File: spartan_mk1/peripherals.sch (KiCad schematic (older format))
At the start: 10 parts

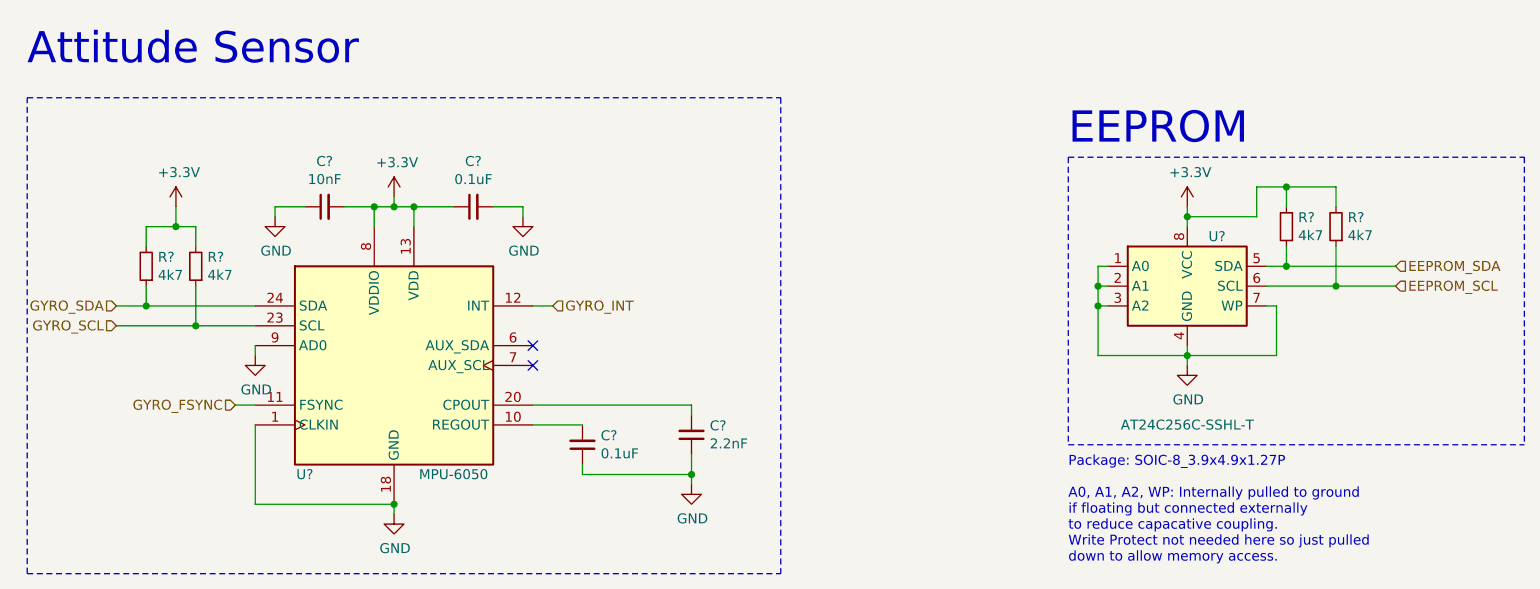
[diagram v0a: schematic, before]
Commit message: Complete schematic with DRC done
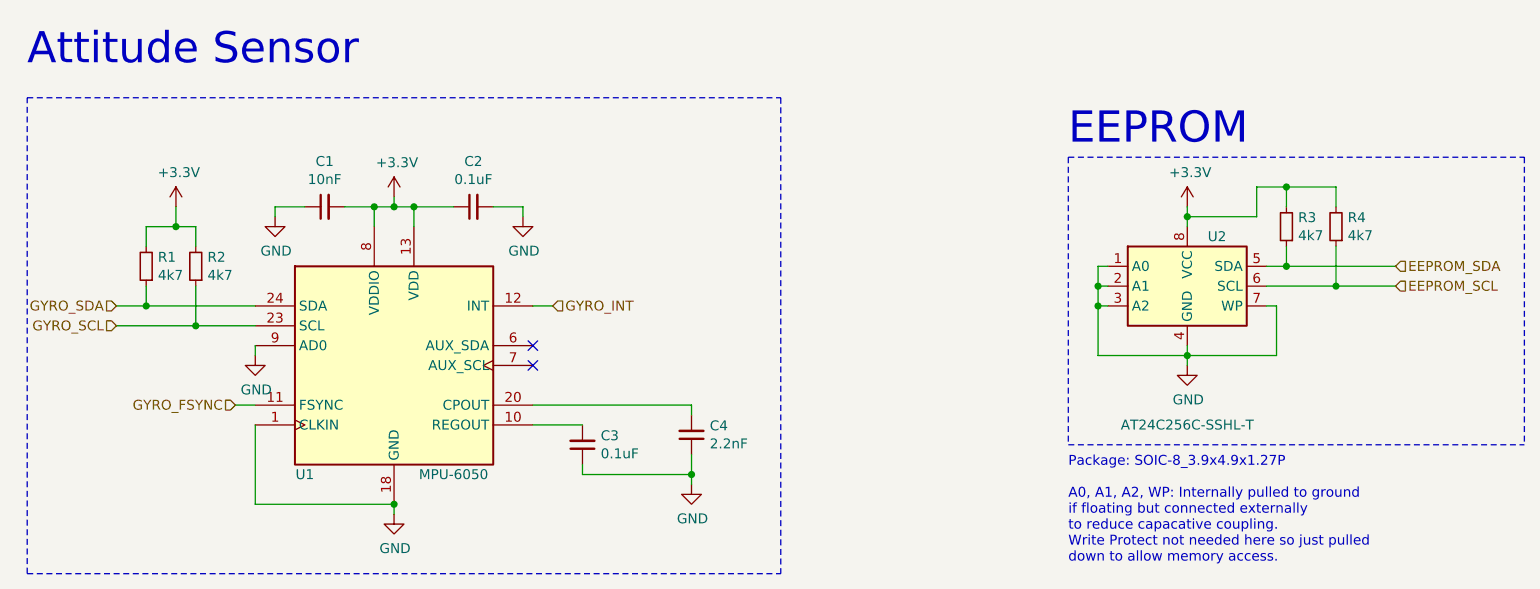
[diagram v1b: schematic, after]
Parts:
- gave numbers to parts that had none: 10
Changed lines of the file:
@@
 	4250 3550 4150 3550
 $Comp
-L Device:C_Small C?
+L Device:C_Small C3
 U 1 1 5F7B41B1
 P 4400 4250
-F 0 "C?" H 4308 4204 50  0000 R CNN
+F 0 "C3" H 4308 4204 50  0000 R CNN
 F 1 "0.1uF" H 4308 4295 50  0000 R CNN
 F 2 "" H 4400 4250 50  0001 C CNN
@@
 $EndComp
 $Comp
-L Device:C_Small C?
+L Device:C_Small C4
 U 1 1 5F7B5CAE
 P 4950 4200
-F 0 "C?" H 4858 4154 50  0000 R CNN
+F 0 "C4" H 4858 4154 50  0000 R CNN
 F 1 "2.2nF" H 4858 4245 50  0000 R CNN
 F 2 "" H 4950 4200 50  0001 C CNN
@@
 	4400 4150 4150 4150
 $Comp
-L Device:C_Small C?
+L Device:C_Small C2
 U 1 1 5F7B64CF
 P 3850 3050
-F 0 "C?" V 4079 3050 50  0000 C CNN
+F 0 "C2" V 4079 3050 50  0000 C CNN
 F 1 "0.1uF" V 3988 3050 50  0000 C CNN
 F 2 "" H 3850 3050 50  0001 C CNN
@@
 $EndComp
 $Comp
-L Device:C_Small C?
+L Device:C_Small C1
 U 1 1 5F7B8C83
 P 3100 3050
-F 0 "C?" V 3329 3050 50  0000 C CNN
+F 0 "C1" V 3329 3050 50  0000 C CNN
 F 1 "10nF" V 3238 3050 50  0000 C CNN
 F 2 "" H 3100 3050 50  0001 C CNN
@@
 $EndComp
 $Comp
-L power:GND #PWR?
+L power:GND #PWR06
 U 1 1 5F7B9C5E
 P 4100 3100
-F 0 "#PWR?" H 4100 2850 50  0001 C CNN
+F 0 "#PWR06" H 4100 2850 50  0001 C CNN
 F 1 "GND" H 4105 2927 50  0000 C CNN
 F 2 "" H 4100 3100 50  0001 C CNN
@@
 	4100 3050 3950 3050
 $Comp
-L power:GND #PWR?
+L power:GND #PWR07
 U 1 1 5F7BA737
 P 4950 4450
-F 0 "#PWR?" H 4950 4200 50  0001 C CNN
+F 0 "#PWR07" H 4950 4200 50  0001 C CNN
 F 1 "GND" H 4955 4277 50  0000 C CNN
 F 2 "" H 4950 4450 50  0001 C CNN
@@
 	4400 4400 4400 4350
 $Comp
-L power:+3.3V #PWR?
+L power:+3.3V #PWR04
 U 1 1 5F7BB185
 P 3450 3000
-F 0 "#PWR?" H 3450 2850 50  0001 C CNN
+F 0 "#PWR04" H 3450 2850 50  0001 C CNN
 F 1 "+3.3V" H 3465 3173 50  0000 C CNN
 F 2 "" H 3450 3000 50  0001 C CNN
@@
 	3350 3050 3200 3050
 $Comp
-L power:GND #PWR?
+L power:GND #PWR03
 U 1 1 5F7BC050
 P 2850 3100
-F 0 "#PWR?" H 2850 2850 50  0001 C CNN
+F 0 "#PWR03" H 2850 2850 50  0001 C CNN
 F 1 "GND" H 2855 2927 50  0000 C CNN
 F 2 "" H 2850 3100 50  0001 C CNN
@@
 	2650 4050 2750 4050
 $Comp
-L power:GND #PWR?
+L power:GND #PWR05
 U 1 1 5F7BD9F9
 P 3450 4600
-F 0 "#PWR?" H 3450 4350 50  0001 C CNN
+F 0 "#PWR05" H 3450 4350 50  0001 C CNN
 F 1 "GND" H 3455 4427 50  0000 C CNN
 F 2 "" H 3450 4600 50  0001 C CNN
@@
 	3450 4550 2750 4550
 $Comp
-L Sensor_Motion:MPU-6050 U?
+L Sensor_Motion:MPU-6050 U1
 U 1 1 5F78649D
 P 3450 3850
-F 0 "U?" H 3000 3300 50  0000 C CNN
+F 0 "U1" H 3000 3300 50  0000 C CNN
 F 1 "MPU-6050" H 3750 3300 50  0000 C CNN
 F 2 "Sensor_Motion:InvenSense_QFN-24_4x4mm_P0.5mm" H 3450 3050 50  0001 C CNN
@@
 $EndComp
 $Comp
-L power:GND #PWR?
+L power:GND #PWR02
 U 1 1 5F993355
 P 2750 3800
-F 0 "#PWR?" H 2750 3550 50  0001 C CNN
+F 0 "#PWR02" H 2750 3550 50  0001 C CNN
 F 1 "GND" H 2755 3627 50  0000 C CNN
 F 2 "" H 2750 3800 50  0001 C CNN
@@
 	2750 3800 2750 3750
 $Comp
-L power:+3.3V #PWR?
+L power:+3.3V #PWR01
 U 1 1 5F993AD9
 P 2350 3050
-F 0 "#PWR?" H 2350 2900 50  0001 C CNN
+F 0 "#PWR01" H 2350 2900 50  0001 C CNN
 F 1 "+3.3V" H 2365 3223 50  0000 C CNN
 F 2 "" H 2350 3050 50  0001 C CNN
@@
 $EndComp
 $Comp
-L Device:R_Small R?
+L Device:R_Small R2
 U 1 1 5F994B07
 P 2450 3350
-F 0 "R?" H 2391 3304 50  0000 R CNN
+F 0 "R2" H 2391 3304 50  0000 R CNN
 F 1 "4k7" H 2391 3395 50  0000 R CNN
 F 2 "" H 2450 3350 50  0001 C CNN
@@
 $EndComp
 $Comp
-L Device:R_Small R?
+L Device:R_Small R1
 U 1 1 5F995818
 P 2200 3350
-F 0 "R?" H 2141 3304 50  0000 R CNN
+F 0 "R1" H 2141 3304 50  0000 R CNN
 F 1 "4k7" H 2141 3395 50  0000 R CNN
 F 2 "" H 2200 3350 50  0001 C CNN
@@
 EEPROM
 $Comp
-L Memory_EEPROM:AT24CS64-SSHM U?
+L Memory_EEPROM:AT24CS64-SSHM U2
 U 1 1 5F9AB042
 P 7450 3450
-F 0 "U?" H 7600 3700 50  0000 C CNN
+F 0 "U2" H 7600 3700 50  0000 C CNN
 F 1 "AT24C256C-SSHL-T" H 7450 2750 50  0000 C CNN
 F 2 "Package_SO:SOIC-8_3.9x4.9mm_P1.27mm" H 7450 3450 50  0001 C CNN
@@
 $EndComp
 $Comp
-L power:GND #PWR?
+L power:GND #PWR09
 U 1 1 5F9AC2AC
 P 7450 3850
-F 0 "#PWR?" H 7450 3600 50  0001 C CNN
+F 0 "#PWR09" H 7450 3600 50  0001 C CNN
 F 1 "GND" H 7455 3677 50  0000 C CNN
 F 2 "" H 7450 3850 50  0001 C CNN
@@
 Package: SOIC-8_3.9x4.9x1.27P\n\nA0, A1, A2, WP: Internally pulled to ground \nif floating but connected externally \nto reduce capacative coupling. \nWrite Protect not needed here so just pulled \ndown to allow memory access.\n
 $Comp
-L power:+3.3V #PWR?
+L power:+3.3V #PWR08
 U 1 1 5F9B2229
 P 7450 3050
-F 0 "#PWR?" H 7450 2900 50  0001 C CNN
+F 0 "#PWR08" H 7450 2900 50  0001 C CNN
 F 1 "+3.3V" H 7465 3223 50  0000 C CNN
 F 2 "" H 7450 3050 50  0001 C CNN
@@
 EEPROM_SCL
 $Comp
-L Device:R_Small R?
+L Device:R_Small R4
 U 1 1 5F9C0959
 P 8200 3150
-F 0 "R?" H 8141 3104 50  0000 R CNN
+F 0 "R4" H 8141 3104 50  0000 R CNN
 F 1 "4k7" H 8141 3195 50  0000 R CNN
 F 2 "" H 8200 3150 50  0001 C CNN
@@
 $EndComp
 $Comp
-L Device:R_Small R?
+L Device:R_Small R3
 U 1 1 5F9C095F
 P 7950 3150
-F 0 "R?" H 7891 3104 50  0000 R CNN
+F 0 "R3" H 7891 3104 50  0000 R CNN
 F 1 "4k7" H 7891 3195 50  0000 R CNN
 F 2 "" H 7950 3150 50  0001 C CNN

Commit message: Footprints added started PCB placement
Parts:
- C1, C2, C3, C4: footprint (none) -> Capacitor_SMD:C_0402_1005Metric
- R1, R2, R3, R4: footprint (none) -> Resistor_SMD:R_0402_1005Metric
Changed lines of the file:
@@
 F 0 "C3" H 4308 4204 50  0000 R CNN
 F 1 "0.1uF" H 4308 4295 50  0000 R CNN
-F 2 "" H 4400 4250 50  0001 C CNN
+F 2 "Capacitor_SMD:C_0402_1005Metric" H 4400 4250 50  0001 C CNN
 F 3 "~" H 4400 4250 50  0001 C CNN
 	1    4400 4250
@@
 F 0 "C4" H 4858 4154 50  0000 R CNN
 F 1 "2.2nF" H 4858 4245 50  0000 R CNN
-F 2 "" H 4950 4200 50  0001 C CNN
+F 2 "Capacitor_SMD:C_0402_1005Metric" H 4950 4200 50  0001 C CNN
 F 3 "~" H 4950 4200 50  0001 C CNN
 	1    4950 4200
@@
 F 0 "C2" V 4079 3050 50  0000 C CNN
 F 1 "0.1uF" V 3988 3050 50  0000 C CNN
-F 2 "" H 3850 3050 50  0001 C CNN
+F 2 "Capacitor_SMD:C_0402_1005Metric" H 3850 3050 50  0001 C CNN
 F 3 "~" H 3850 3050 50  0001 C CNN
 	1    3850 3050
@@
 F 0 "C1" V 3329 3050 50  0000 C CNN
 F 1 "10nF" V 3238 3050 50  0000 C CNN
-F 2 "" H 3100 3050 50  0001 C CNN
+F 2 "Capacitor_SMD:C_0402_1005Metric" H 3100 3050 50  0001 C CNN
 F 3 "~" H 3100 3050 50  0001 C CNN
 	1    3100 3050
@@
 F 0 "R2" H 2391 3304 50  0000 R CNN
 F 1 "4k7" H 2391 3395 50  0000 R CNN
-F 2 "" H 2450 3350 50  0001 C CNN
+F 2 "Resistor_SMD:R_0402_1005Metric" H 2450 3350 50  0001 C CNN
 F 3 "~" H 2450 3350 50  0001 C CNN
 	1    2450 3350
@@
 F 0 "R1" H 2141 3304 50  0000 R CNN
 F 1 "4k7" H 2141 3395 50  0000 R CNN
-F 2 "" H 2200 3350 50  0001 C CNN
+F 2 "Resistor_SMD:R_0402_1005Metric" H 2200 3350 50  0001 C CNN
 F 3 "~" H 2200 3350 50  0001 C CNN
 	1    2200 3350
@@
 F 0 "R4" H 8141 3104 50  0000 R CNN
 F 1 "4k7" H 8141 3195 50  0000 R CNN
-F 2 "" H 8200 3150 50  0001 C CNN
+F 2 "Resistor_SMD:R_0402_1005Metric" H 8200 3150 50  0001 C CNN
 F 3 "~" H 8200 3150 50  0001 C CNN
 	1    8200 3150
@@
 F 0 "R3" H 7891 3104 50  0000 R CNN
 F 1 "4k7" H 7891 3195 50  0000 R CNN
-F 2 "" H 7950 3150 50  0001 C CNN
+F 2 "Resistor_SMD:R_0402_1005Metric" H 7950 3150 50  0001 C CNN
 F 3 "~" H 7950 3150 50  0001 C CNN
 	1    7950 3150

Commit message: Generated gerber files. Positions and BOM assemly files generated
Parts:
- C1: LCSC (none) -> C15195; LCSC Part # (none) -> C15195
- C2, C3: LCSC (none) -> C1525; LCSC Part # (none) -> C1525
- C4: LCSC (none) -> C1531; LCSC Part # (none) -> C1531
- R1, R2, R3, R4: LCSC (none) -> C25900; LCSC Part # (none) -> C25900
- U1: LCSC (none) -> C24112; LCSC Part # (none) -> C24112
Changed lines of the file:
@@
 F 2 "Capacitor_SMD:C_0402_1005Metric" H 4400 4250 50  0001 C CNN
 F 3 "~" H 4400 4250 50  0001 C CNN
+F 4 "C1525" H 4400 4250 50  0001 C CNN "LCSC Part #"
+F 5 "C1525" H 4400 4250 50  0001 C CNN "LCSC"
 	1    4400 4250
 	-1   0    0    1
@@
 F 2 "Capacitor_SMD:C_0402_1005Metric" H 4950 4200 50  0001 C CNN
 F 3 "~" H 4950 4200 50  0001 C CNN
+F 4 "C1531" H 4950 4200 50  0001 C CNN "LCSC Part #"
+F 5 "C1531" H 4950 4200 50  0001 C CNN "LCSC"
 	1    4950 4200
 	-1   0    0    1
@@
 F 2 "Capacitor_SMD:C_0402_1005Metric" H 3850 3050 50  0001 C CNN
 F 3 "~" H 3850 3050 50  0001 C CNN
+F 4 "C1525" H 3850 3050 50  0001 C CNN "LCSC Part #"
+F 5 "C1525" H 3850 3050 50  0001 C CNN "LCSC"
 	1    3850 3050
 	0    -1   -1   0
@@
 F 2 "Capacitor_SMD:C_0402_1005Metric" H 3100 3050 50  0001 C CNN
 F 3 "~" H 3100 3050 50  0001 C CNN
+F 4 "C15195" H 3100 3050 50  0001 C CNN "LCSC Part #"
+F 5 "C15195" H 3100 3050 50  0001 C CNN "LCSC"
 	1    3100 3050
 	0    -1   -1   0
@@
 F 2 "Sensor_Motion:InvenSense_QFN-24_4x4mm_P0.5mm" H 3450 3050 50  0001 C CNN
 F 3 "https://store.invensense.com/datasheets/invensense/MPU-6050_DataSheet_V3%204.pdf" H 3450 3700 50  0001 C CNN
+F 4 "C24112" H 3450 3850 50  0001 C CNN "LCSC Part #"
+F 5 "C24112" H 3450 3850 50  0001 C CNN "LCSC"
 	1    3450 3850
 	1    0    0    -1
@@
 F 2 "Resistor_SMD:R_0402_1005Metric" H 2450 3350 50  0001 C CNN
 F 3 "~" H 2450 3350 50  0001 C CNN
+F 4 "C25900" H 2450 3350 50  0001 C CNN "LCSC Part #"
+F 5 "C25900" H 2450 3350 50  0001 C CNN "LCSC"
 	1    2450 3350
 	-1   0    0    1
@@
 F 2 "Resistor_SMD:R_0402_1005Metric" H 2200 3350 50  0001 C CNN
 F 3 "~" H 2200 3350 50  0001 C CNN
+F 4 "C25900" H 2200 3350 50  0001 C CNN "LCSC Part #"
+F 5 "C25900" H 2200 3350 50  0001 C CNN "LCSC"
 	1    2200 3350
 	-1   0    0    1
@@
 F 2 "Resistor_SMD:R_0402_1005Metric" H 8200 3150 50  0001 C CNN
 F 3 "~" H 8200 3150 50  0001 C CNN
+F 4 "C25900" H 8200 3150 50  0001 C CNN "LCSC Part #"
+F 5 "C25900" H 8200 3150 50  0001 C CNN "LCSC"
 	1    8200 3150
 	-1   0    0    1
@@
 F 2 "Resistor_SMD:R_0402_1005Metric" H 7950 3150 50  0001 C CNN
 F 3 "~" H 7950 3150 50  0001 C CNN
+F 4 "C25900" H 7950 3150 50  0001 C CNN "LCSC Part #"
+F 5 "C25900" H 7950 3150 50  0001 C CNN "LCSC"
 	1    7950 3150
 	-1   0    0    1
